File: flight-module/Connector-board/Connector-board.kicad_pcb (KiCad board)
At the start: 4 copper layers, 134.1 x 141.7 mm, 42 parts, among them J1 Stack_Shape, U1 MAX31855KASA, U2 MAX31855KASA, U3 MAX31855KASA, U4 MAX31855KASA

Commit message: merge conflict fix
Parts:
- D7, D8: value D_Schottky -> Flyback_Diode; footprint Diode_SMD:D_SOD-128 -> Diode_SMD:CUHS20S40H3F
- PT_DSUB1: footprint Connector_Dsub:DSUB-25_Male_Vertical_P2.77x2.84mm_MountingHoles -> Connector_Dsub:DSUB-25_Female_Vertical_P2.77x2.84mm_MountingHoles
- moved G*** 8.04 mm to (208.3, 95.2), turned to 90 degrees
- moved PT_DSUB1 2.98 mm to (156.2, 78.5), turned to 180 degrees
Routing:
- net PT1_E-: track 30.1 -> 23.8 mm
- net PT5_E-: track 61.7 -> 67.6 mm
- net PT1_E+: track 29.7 -> 24.7 mm
- net PT6_E-: track 35.2 -> 30.4 mm, vias 1 -> 0
- net PT1_A+: track 24.4 -> 29.1 mm
- net GND: track 58.5 -> 63.2 mm
- net PT4_A+: track 27.5 -> 31.3 mm
- net PT3_A+: track 26.5 -> 30.4 mm
- net PT2_A+: track 25.4 -> 29.2 mm
- net PT6_A+: track 25.8 -> 29.4 mm
- net PT5_A+: track 52.4 -> 55.3 mm
- net PT6_E+: track 41.0 -> 38.8 mm
- net PT4_E+: track 29.2 -> 27.1 mm
- net PT2_E-: track 26.9 -> 24.8 mm, vias 1 -> 0
- net PT4_E-: track 28.9 -> 26.8 mm
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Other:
- board text added: "TC 1"
- board text added: "TC 2"
- board text added: "TC 3"
- board text added: "TC 4"
- board text added: "WRONG SIDE"

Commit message: final boards orderedd
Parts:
- D7, D8: value Flyback_Diode -> D_Schottky; footprint Diode_SMD:CUHS20S40H3F -> Diode_SMD:D_SOD-128
- PT_DSUB1: footprint Connector_Dsub:DSUB-25_Female_Vertical_P2.77x2.84mm_MountingHoles -> Connector_Dsub:DSUB-25_Male_Vertical_P2.77x2.84mm_MountingHoles
- moved C6 13.6 mm to (152.4, 110.4), turned to -90 degrees
- moved C8 13.5 mm to (142.2, 111.0), turned to -90 degrees
- moved C10 13.0 mm to (132.0, 110.4), turned to -90 degrees
- moved C4 12.6 mm to (121.9, 110.2), turned to -90 degrees
- moved G*** 8.04 mm to (212.0, 88.1), turned to 0 degrees
- moved PT_DSUB1 2.98 mm to (157.5, 81.1), turned to 0 degrees
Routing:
- net +3.3V: track 181.0 -> 124.6 mm, vias 4 -> 2
- net GND: track 63.2 -> 52.2 mm, vias 17 -> 13
- net PT1_E-: track 23.8 -> 30.1 mm
- net PT5_E-: track 67.6 -> 61.7 mm
- net PT1_E+: track 24.7 -> 29.7 mm
- net PT6_E-: track 30.4 -> 35.2 mm, vias 0 -> 1
- net PT1_A+: track 29.1 -> 24.4 mm
- net PT4_A+: track 31.3 -> 27.5 mm
- net PT3_A+: track 30.4 -> 26.5 mm
- net PT2_A+: track 29.2 -> 25.4 mm
- net PT6_A+: track 29.4 -> 25.8 mm
- net PT5_A+: track 55.3 -> 52.4 mm
- net PT6_E+: track 38.8 -> 41.0 mm
- net PT4_E+: track 27.1 -> 29.2 mm
- net PT2_E-: track 24.8 -> 26.9 mm, vias 0 -> 1
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- added copper zone on F.Cu, net GND
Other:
- board text removed: "TC 1"
- board text removed: "TC 2"
- board text removed: "TC 3"
- board text removed: "TC 4"
- board text removed: "WRONG SIDE"

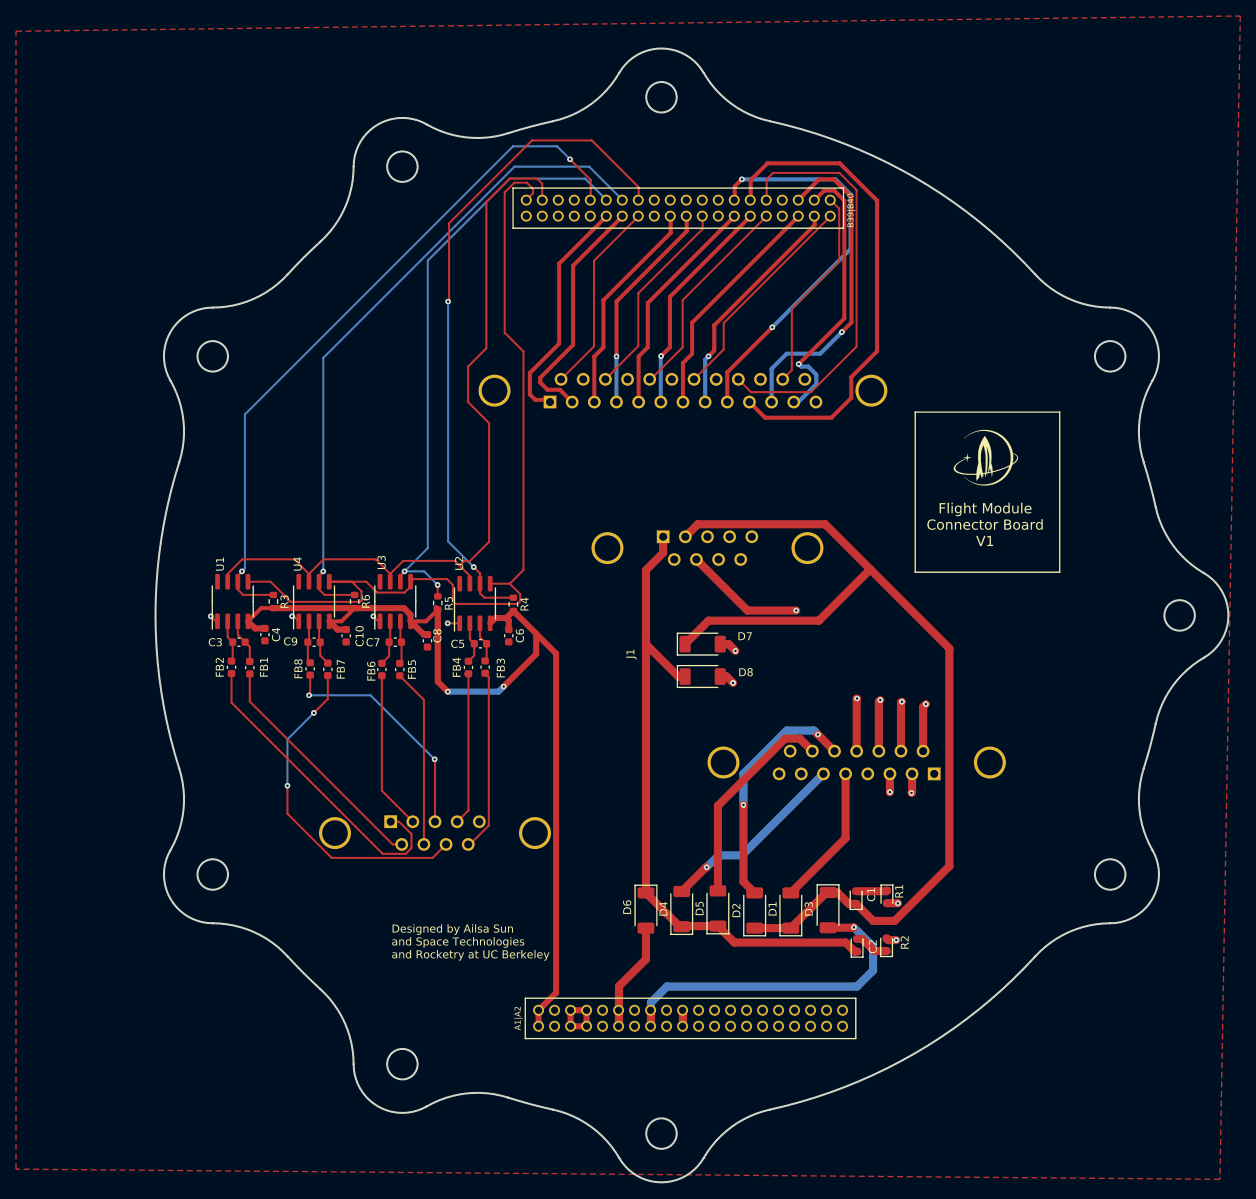
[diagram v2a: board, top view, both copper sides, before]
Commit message: finished the connector board
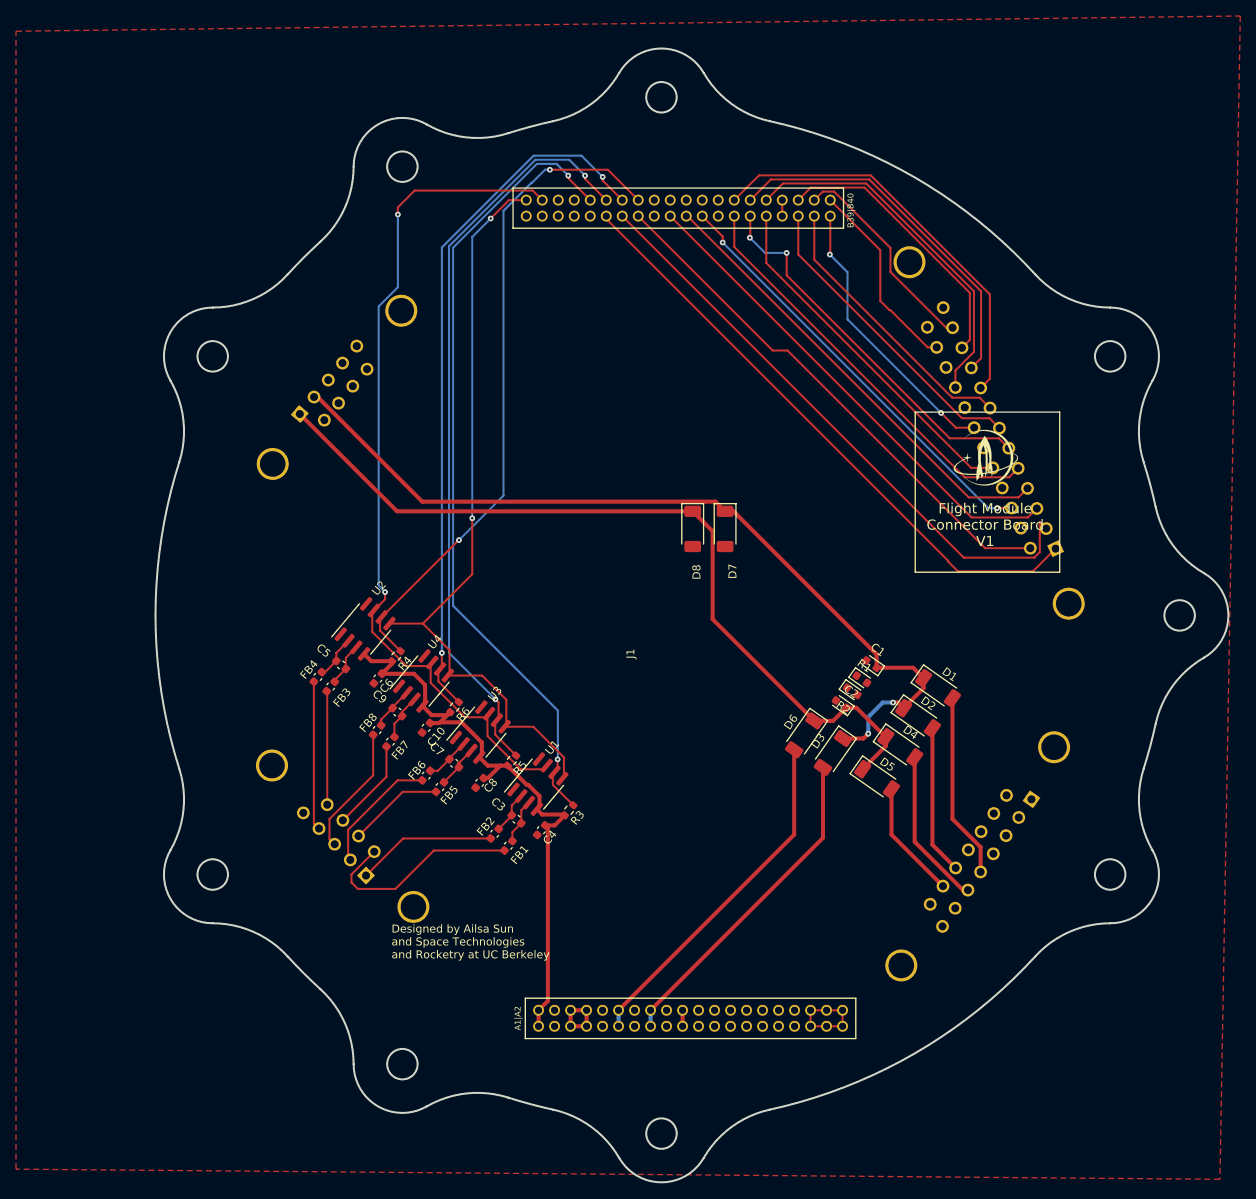
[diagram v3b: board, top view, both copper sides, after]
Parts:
- moved PT_DSUB1 65.8 mm to (220.7, 99.5), turned to 115 degrees
- moved SOLENOIDS_DSUB1 47.9 mm to (126.2, 82.6), turned to -130 degrees
- moved R3 45.2 mm to (159.9, 132.2), turned to -130 degrees
- moved U1 44.4 mm to (156.0, 128.9), turned to 50 degrees
- moved C4 42.3 mm to (156.4, 134.7), turned to -130 degrees
- moved C3 41.2 mm to (153.3, 133.3), turned to 140 degrees
- moved FB1 39.2 mm to (152.3, 136.6), turned to 50 degrees
- moved FB2 38.9 mm to (150.6, 135.1), turned to 50 degrees
- moved D4 34.0 mm to (201.3, 124.3), turned to -35 degrees
- moved D1 33.3 mm to (206.0, 116.9), turned to -35 degrees
- moved R2 32.0 mm to (195.3, 117.3), turned to -35 degrees
- moved D2 31.5 mm to (203.5, 120.7), turned to -35 degrees
- moved C2 30.2 mm to (193.9, 118.9), turned to 145 degrees
- moved D6 29.5 mm to (189.3, 122.8), turned to -125 degrees
- moved C1 29.2 mm to (197.7, 113.9), turned to 145 degrees
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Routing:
- net GND: track 52.2 -> 2.00 mm, vias 13 -> 0
- net +3.3V: track 124.6 -> 76.5 mm, vias 2 -> 0
- net PT1_E+: track 29.7 -> 76.0 mm
- net PT1_E-: track 30.1 -> 75.1 mm
- net PT1_A+: track 24.4 -> 66.2 mm
- net PT2_E+: track 27.2 -> 61.9 mm
- net PT2_E-: track 26.9 -> 57.7 mm, vias 1 -> 0
- net TC3_T+: track 42.2 -> 11.5 mm, vias 2 -> 0
- net FLIGHT_LOX_VENT: track 13.7 -> 43.7 mm
- net PT2_A+: track 25.4 -> 54.2 mm, vias 0 -> 2
- net PT3_E+: track 28.2 -> 51.7 mm
- net TC1_T-: track 39.3 -> 17.5 mm
- net LOX_VENT: track 82.6 -> 103.0 mm
- net PT3_E-: track 27.9 -> 47.6 mm, vias 1 -> 2
- net PT3_A+: track 26.5 -> 44.8 mm
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
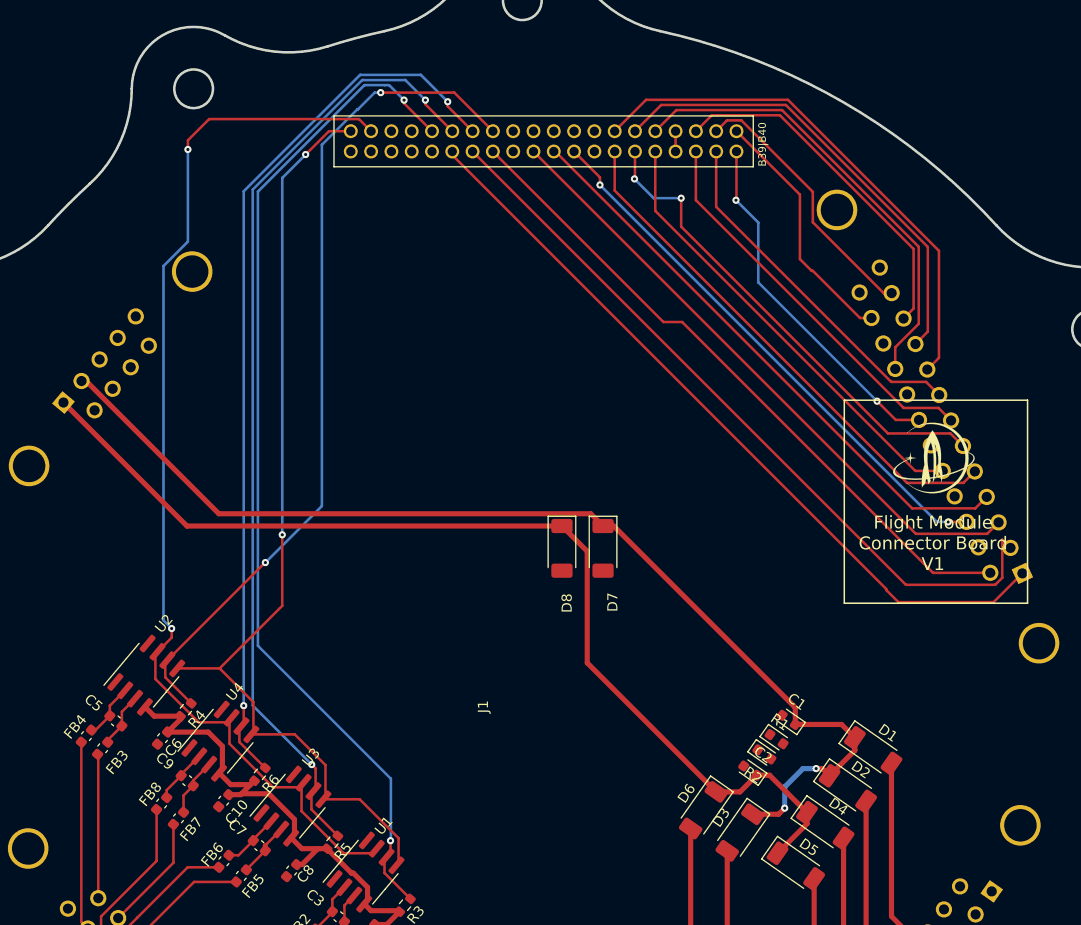
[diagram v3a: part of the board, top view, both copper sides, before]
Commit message: connector fix - change to SMD
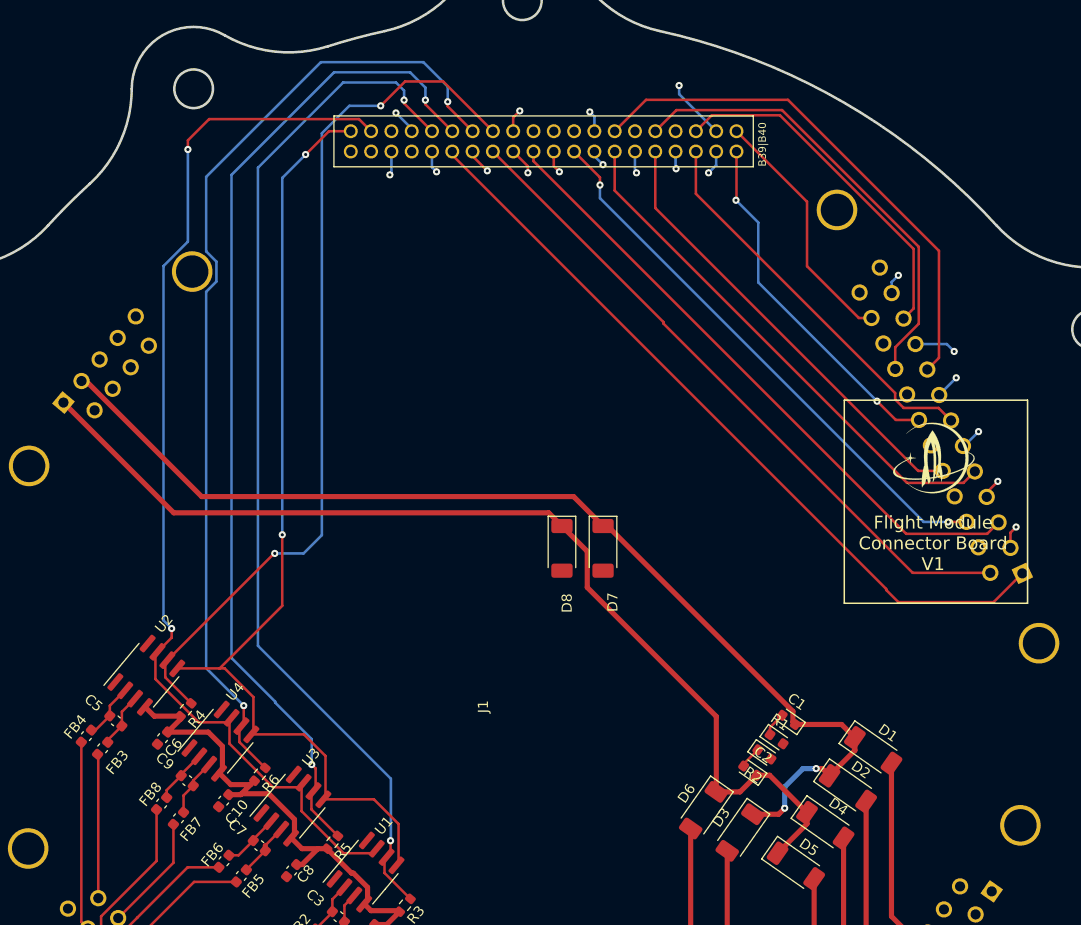
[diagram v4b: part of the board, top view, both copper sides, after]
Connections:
- C10 pad 2: GND -> PT1_E-
- C4 pad 2: GND -> PT1_E-
- C6 pad 2: GND -> PT1_E-
- C8 pad 2: GND -> PT1_E-
- D7 pad 2: GND -> PT1_E-
- D8 pad 2: GND -> PT1_E-
- GND_DSUB1 pad 10: GND -> PT1_E-
- GND_DSUB1 pad 11: GND -> PT1_E-
- GND_DSUB1 pad 12: GND -> PT1_E-
- GND_DSUB1 pad 9: GND -> PT1_E-
- J1 pad A10: GND -> PT1_E-
- J1 pad A13: GND -> PT1_E-
- J1 pad A14: GND -> PT1_E-
- J1 pad A17: GND -> PT1_E-
- J1 pad A18: GND -> PT1_E-
- J1 pad A21: GND -> PT1_E-
- J1 pad A22: GND -> PT1_E-
- J1 pad A25: GND -> PT1_E-
- J1 pad A26: GND -> PT1_E-
- J1 pad A3: GND -> PT1_E-
- J1 pad A4: GND -> PT1_E-
- J1 pad A9: GND -> PT1_E-
- J1 pad B17: GND -> PT1_E-
- J1 pad B18: GND -> PT1_E-
- J1 pad B21: PT2_E- -> PT1_E-
- J1 pad B25: GND -> PT1_E-
- J1 pad B26: GND -> PT1_E-
- J1 pad B29: PT3_E- -> PT1_E-
- J1 pad B30: PT5_E- -> PT1_E-
- J1 pad B33: GND -> PT1_E-
- J1 pad B34: GND -> PT1_E-
- J1 pad B37: PT4_E- -> PT1_E-
- J1 pad B38: PT6_E- -> PT1_E-
- J1 pad B5: GND -> PT1_E-
- J1 pad B8: GND -> PT1_E-
- J1 pad B9: GND -> PT1_E-
- PT_DSUB1 pad 10: PT5_E- -> PT1_E-
- PT_DSUB1 pad 12: PT6_E- -> PT1_E-
- PT_DSUB1 pad 4: PT2_E- -> PT1_E-
- PT_DSUB1 pad 6: PT3_E- -> PT1_E-
- PT_DSUB1 pad 8: PT4_E- -> PT1_E-
- R1 pad 2: GND -> PT1_E-
- R2 pad 2: GND -> PT1_E-
- SOLENOIDS_DSUB1 pad 6: GND -> PT1_E-
- SOLENOIDS_DSUB1 pad 7: GND -> PT1_E-
- U1 pad 1: GND -> PT1_E-
- U2 pad 1: GND -> PT1_E-
- U3 pad 1: GND -> PT1_E-
- U4 pad 1: GND -> PT1_E-
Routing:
- net PT2_E-: track 57.7 -> 0.00 mm
- net PT3_E-: track 47.6 -> 0.00 mm, vias 2 -> 0
- net PT5_E-: track 45.8 -> 0.00 mm
- net PT4_E-: track 35.1 -> 0.00 mm
- net PT1_E-: track 75.1 -> 48.0 mm, vias 0 -> 19
- net PT6_E-: track 26.5 -> 0.00 mm
- net TC3_CS: track 87.9 -> 96.7 mm
- net TC2_CS: track 94.0 -> 99.1 mm
- net TC4_CS: track 83.1 -> 86.3 mm
- net Net-(C1-Pad2): track 0.00 -> 2.40 mm
- net Net-(C2-Pad2): track 0.00 -> 2.18 mm
- net TC1_CS: track 100.1 -> 102.2 mm
- net GND: track 2.00 -> 0.00 mm
- net SPI_SCK: track 95.4 -> 97.1 mm
- net PT2_A+: track 54.2 -> 55.0 mm
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- added copper zone on F.Cu, net PT1_E-
- added copper zone on In1.Cu, net PT1_E-
- removed copper zone on F.Cu, net GND
- removed copper zone on In1.Cu, net GND

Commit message: connector board updates for manufacturing
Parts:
- moved G*** 40.3 mm to (173.9, 74.8)
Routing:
- net PT1_E-: track 48.0 -> 80.6 mm, vias 19 -> 31
- removed copper zone on F.Cu, net PT1_E-

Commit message: connector gerbs
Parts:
- PT_DSUB1: footprint Connector_Dsub:DSUB-25_Male_Vertical_P2.77x2.84mm_MountingHoles -> Connector_Dsub:DSUB-25_Female_Vertical_P2.77x2.84mm_MountingHoles
- moved PT_DSUB1 33.2 mm to (206.7, 69.4)
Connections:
- J1 pad A5: +5V -> PT1_E+
- J1 pad A6: +5V -> PT1_E+
- J1 pad A7: +5V -> PT1_E+
- J1 pad A8: +5V -> PT1_E+
- J1 pad B19: PT2_E+ -> PT1_E+
- J1 pad B27: PT3_E+ -> PT1_E+
- J1 pad B28: PT5_E+ -> PT1_E+
- J1 pad B35: PT4_E+ -> PT1_E+
- J1 pad B36: PT6_E+ -> PT1_E+
- PT_DSUB1 pad 11: PT6_E+ -> PT1_E+
- PT_DSUB1 pad 3: PT2_E+ -> PT1_E+
- PT_DSUB1 pad 5: PT3_E+ -> PT1_E+
- PT_DSUB1 pad 7: PT4_E+ -> PT1_E+
- PT_DSUB1 pad 9: PT5_E+ -> PT1_E+
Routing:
- net PWR_SUP: track 12.0 -> 100.4 mm
- net PT1_E+: track 76.0 -> 0.00 mm
- net PT2_E+: track 62.5 -> 0.00 mm
- net PT3_E+: track 51.7 -> 0.00 mm
- net PT5_E+: track 51.6 -> 0.00 mm
- net PT4_E+: track 38.9 -> 0.00 mm
- net PT6_E+: track 34.8 -> 0.00 mm
- net PT6_A+: track 24.6 -> 55.8 mm
- net PT1_E-: track 80.6 -> 50.0 mm, vias 31 -> 18
- net PT1_A+: track 66.3 -> 46.1 mm, vias 0 -> 1
- net PT5_A+: track 45.4 -> 60.2 mm
- net PT2_A+: track 55.0 -> 44.2 mm, vias 2 -> 1
- net PT4_A+: track 35.3 -> 43.8 mm, vias 2 -> 1
- net +5V: track 8.00 -> 0.00 mm
- net PT3_A+: track 44.6 -> 44.2 mm, vias 0 -> 1
- added copper zone on In2.Cu, net PT1_E+
- removed copper zone on In2.Cu, net PWR_SUP
